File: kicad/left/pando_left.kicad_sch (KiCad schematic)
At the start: 84 parts, among them J1 USB_C_Receptacle_USB2.0_14P, J2 USB_C_Receptacle_USB2.0_14P, U1 STM32G0B1CBT6, U2 PRTR5V0U2X, U3 XC6206PxxxMR-Regulator_Linear, U4 PRTR5V0U2X

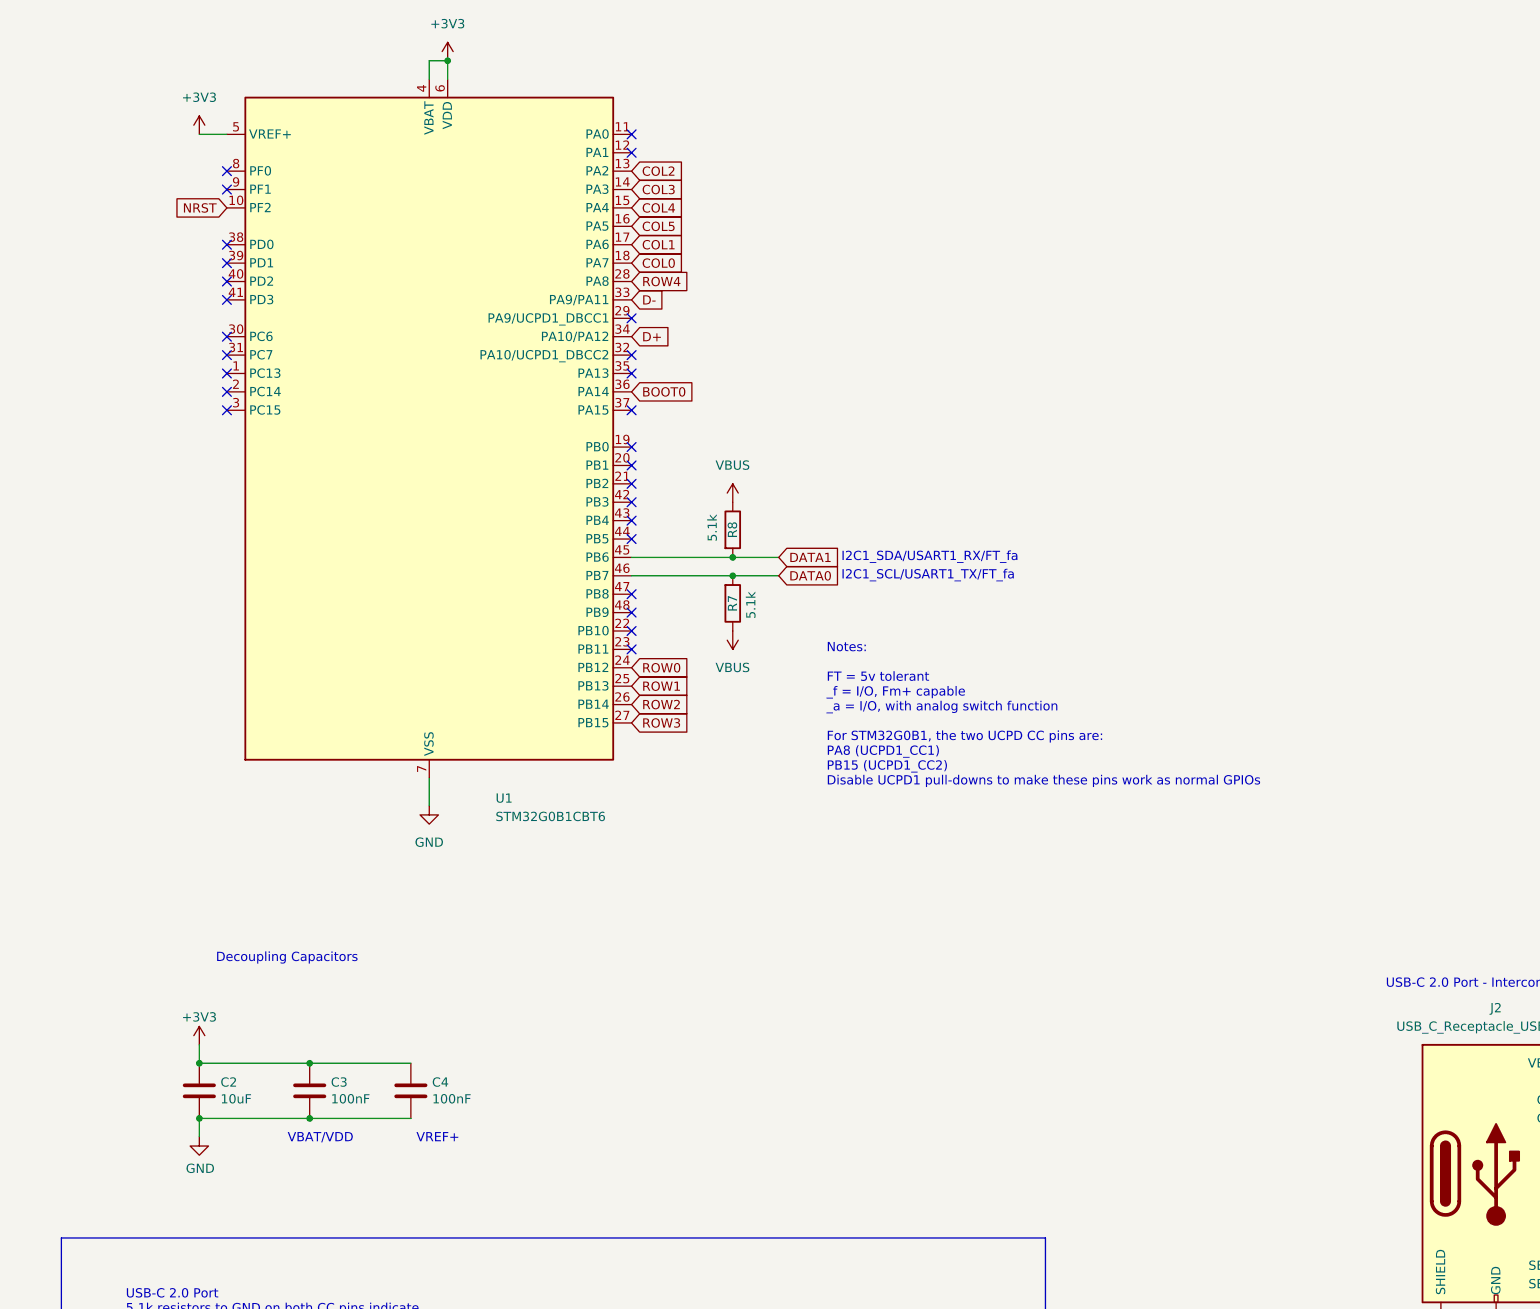
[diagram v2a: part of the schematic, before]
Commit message: Update left PCB and schematic for STM32G0B1KBT6
Replace STM32G0B1CBT6 with STM32G0B1KBT6 MCU. Update routing
and schematics to match new pinout and requirements.
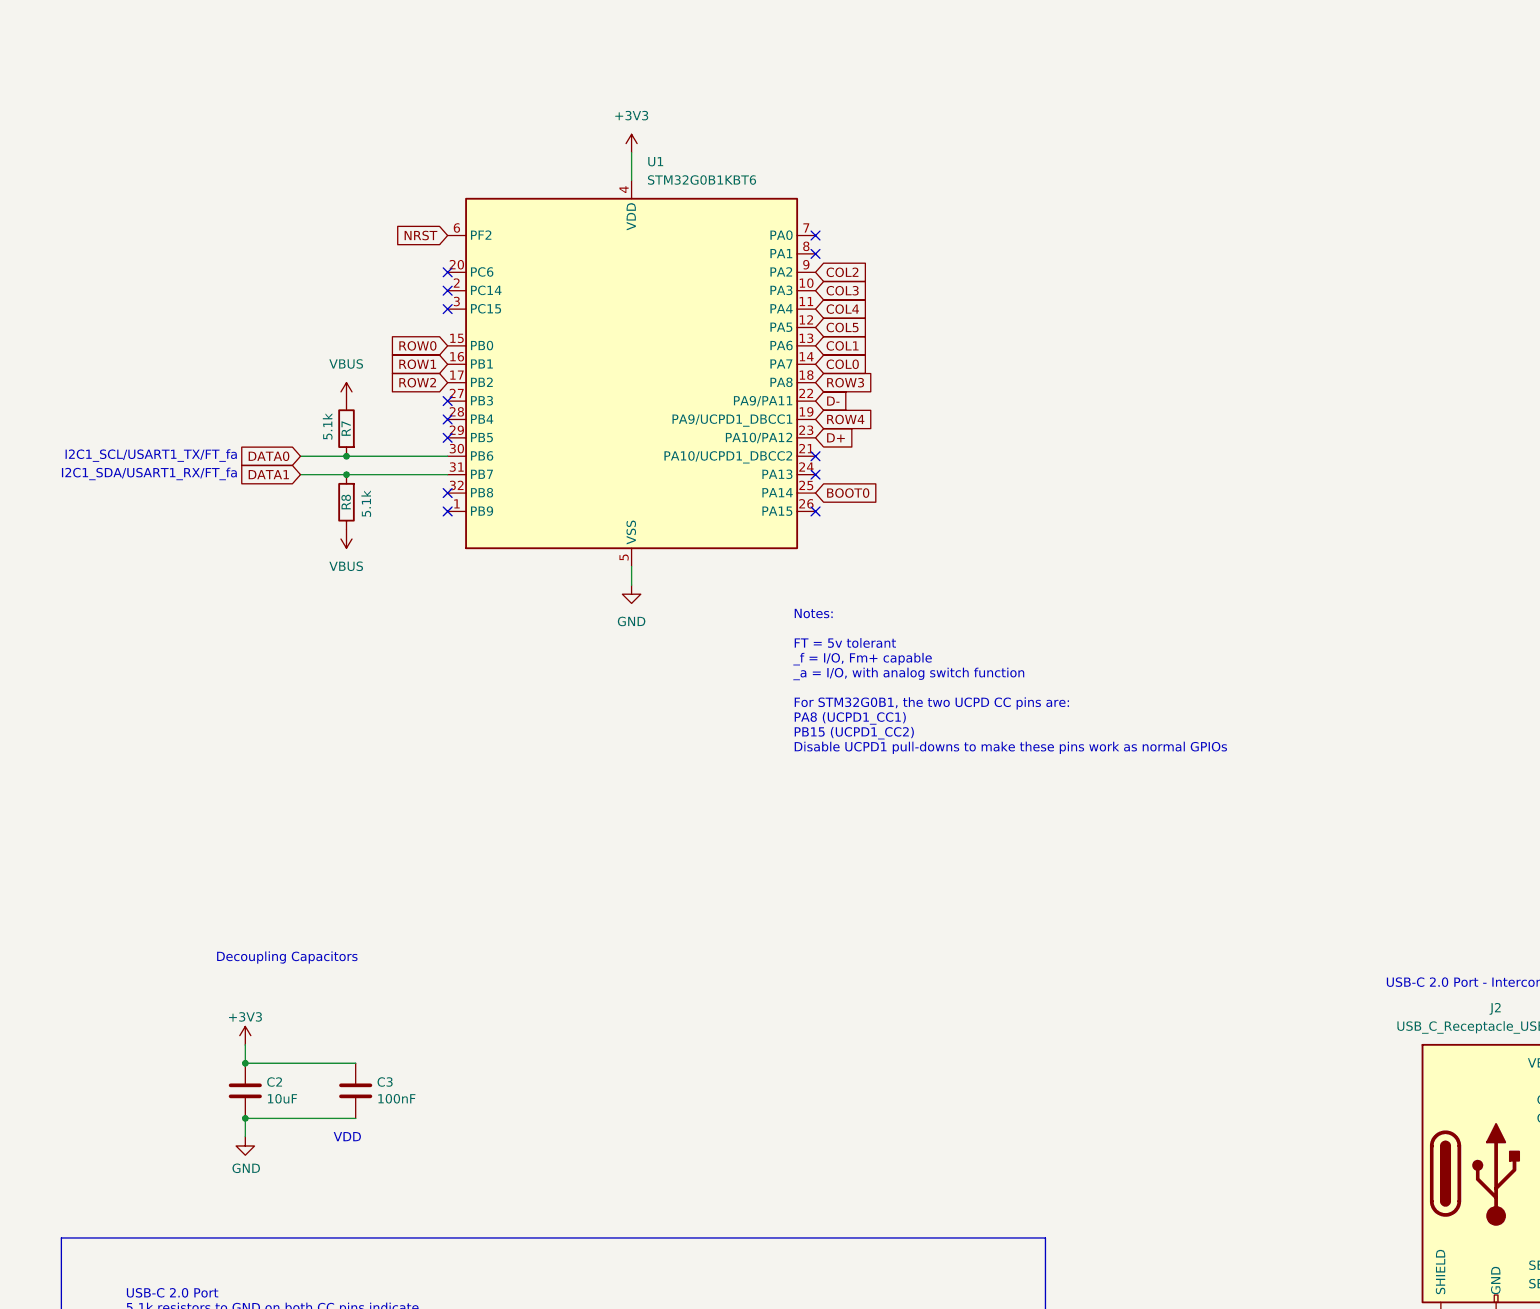
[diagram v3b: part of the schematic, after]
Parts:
- removed C4: 100nF, Capacitor_SMD:C_0603_1608Metric, symbol Device:C
- removed U1: STM32G0B1CBT6, Package_QFP:LQFP-48_7x7mm_P0.5mm, symbol MCU_ST_STM32G0:STM32G0B1CBTx
- added U1: STM32G0B1KBT6, Package_QFP:LQFP-32_7x7mm_P0.8mm, symbol MCU_ST_STM32G0:STM32G0B1KBTx
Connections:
- net +3V3: now also U1.4 (VDD)
- net BOOT0: now also U1.25 (PA14)
- net COL0: now also U1.14 (PA7)
- net COL1: now also U1.13 (PA6)
- net COL2: now also U1.9 (PA2)
- net COL3: now also U1.10 (PA3)
- net COL4: now also U1.11 (PA4)
- net COL5: now also U1.12 (PA5)
- net D+: now also U1.23 (PA10/PA12)
- net D-: now also U1.22 (PA9/PA11)
- net DATA0: now also U1.30 (PB6)
- net DATA1: now also U1.31 (PB7)
- net GND: now also U1.5 (VSS)
- net NRST: now also U1.6 (PF2)
- net ROW0: now also U1.15 (PB0)
- net ROW1: now also U1.16 (PB1)
- net ROW2: now also U1.17 (PB2)
- net ROW3: now also U1.18 (PA8)
- net ROW4: now also U1.19 (PA9/UCPD1_DBCC1)
- no-connect marks 31 -> 17
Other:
- note added: "VDD"
- note removed: "VBAT/VDD"
- note removed: "VREF+"
- moved on the sheet: C2, C3
